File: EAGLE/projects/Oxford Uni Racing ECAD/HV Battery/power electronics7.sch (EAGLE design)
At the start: 49 parts, among them IC1 4043D, IC2 SE555D, IC6 4011D, K1 T9AS1D12-48=T9A, K2 T9AS5D12-12=T9A, K3 T9AS1D12-48=T9A, K4 T9AS1D12-48=T9A, K5 T9AS1D12-48=T9A, Q1 BSS138, Q2 BSS138, Q3 BSS138

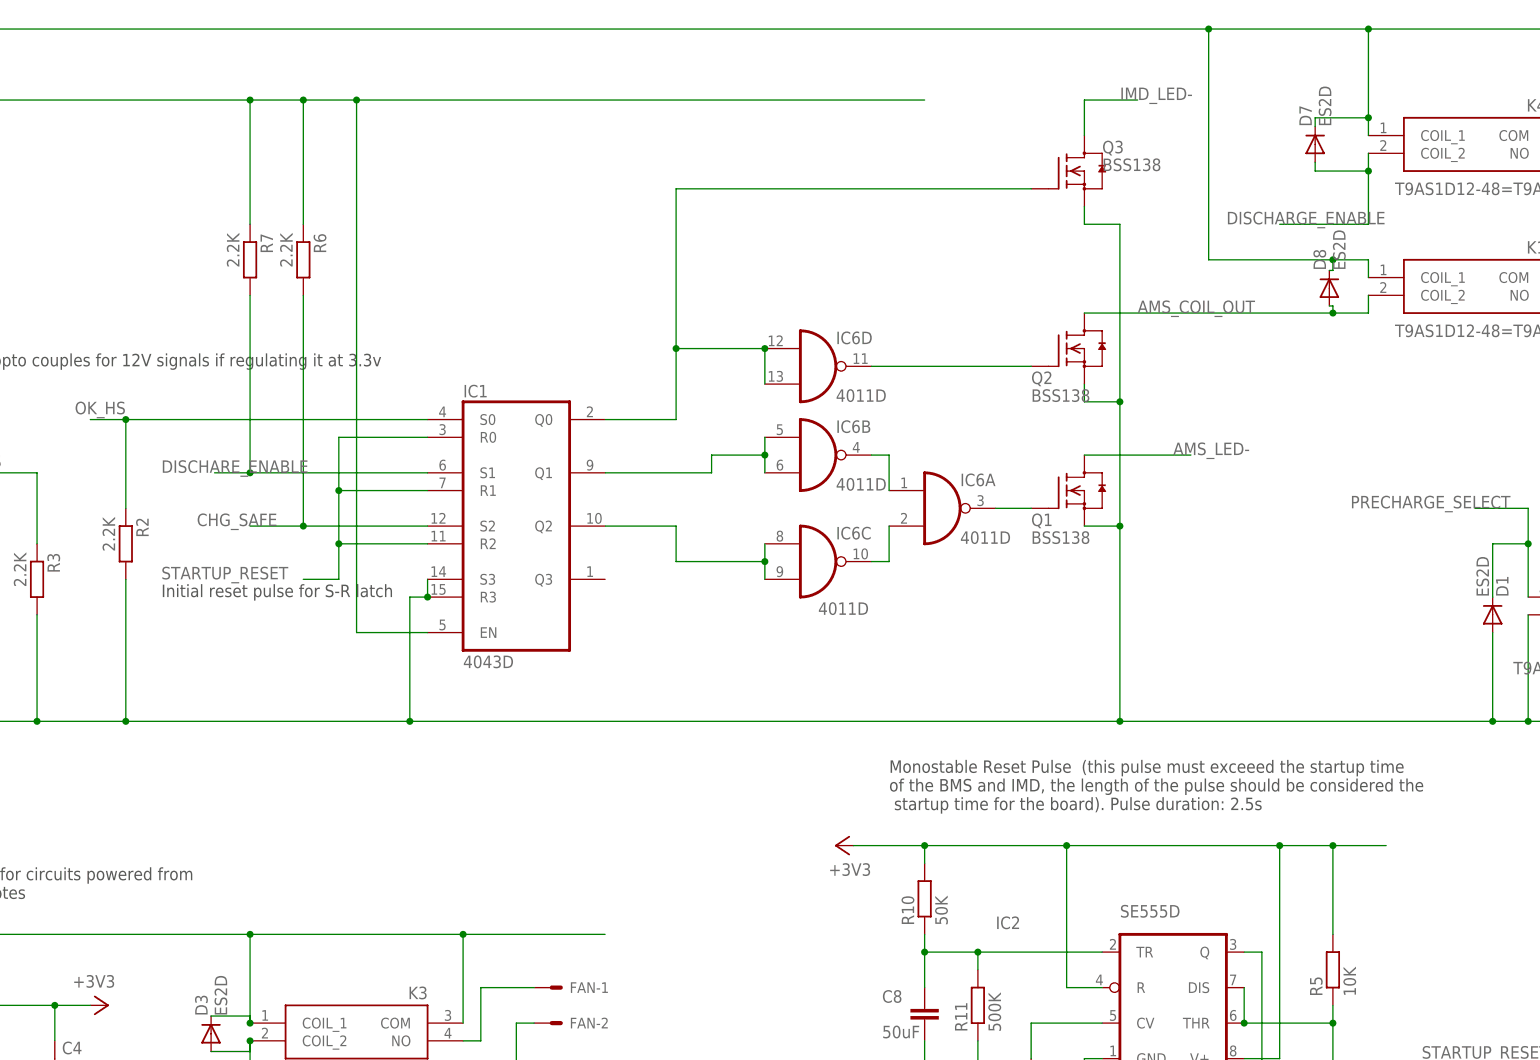
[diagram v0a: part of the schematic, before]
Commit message: added wills suggestions and test pads
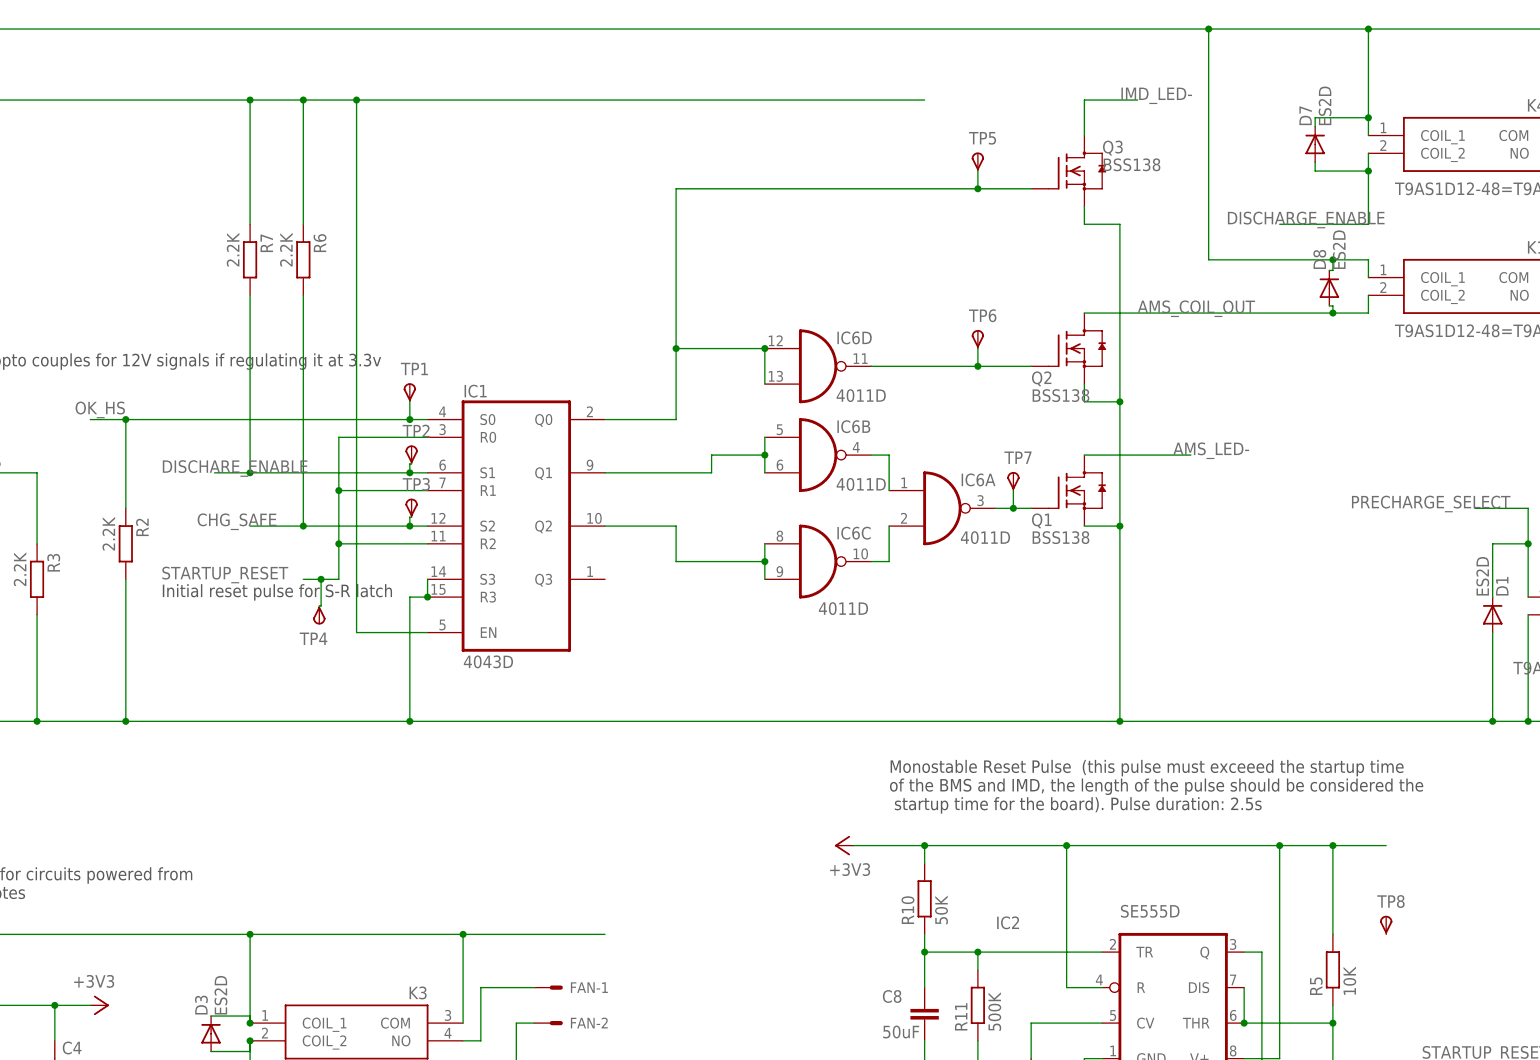
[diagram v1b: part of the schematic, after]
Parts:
- added TP1, TP2, TP3, TP4, TP5, TP6, TP7: TPSTP11R, testpad:TPSTP11R
- added TP8: TPSTP17R, testpad:TPSTP17R
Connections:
- net CHG_SAFE: now also TP3.PP
- net DISCHARE_ENABLE: now also TP2.PP
- net N$21: now also TP7.PP
- net N$37: now also TP6.PP
- net N$8: now also TP5.PP
- net OK_HS: now also TP1.PP
- net STARTUP_RESET: now also TP4.PP
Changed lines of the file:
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@@
 <part name="FAN" library="con-molex" library_urn="urn:adsk.eagle:library:165" deviceset="KK-156-2" device=""/>
 <part name="D3" library="diode" library_urn="urn:adsk.eagle:library:210" deviceset="ES2D" device="" package3d_urn="urn:adsk.eagle:package:43404/2"/>
+<part name="TP1" library="testpad" library_urn="urn:adsk.eagle:library:385" deviceset="TPS" device="TP11R" package3d_urn="urn:adsk.eagle:package:27961/1" value="TPSTP11R"/>
+<part name="TP2" library="testpad" library_urn="urn:adsk.eagle:library:385" deviceset="TPS" device="TP11R" package3d_urn="urn:adsk.eagle:package:27961/1" value="TPSTP11R"/>
+<part name="TP3" library="testpad" library_urn="urn:adsk.eagle:library:385" deviceset="TPS" device="TP11R" package3d_urn="urn:adsk.eagle:package:27961/1" value="TPSTP11R"/>
+<part name="TP5" library="testpad" library_urn="urn:adsk.eagle:library:385" deviceset="TPS" device="TP11R" package3d_urn="urn:adsk.eagle:package:27961/1" value="TPSTP11R"/>
+<part name="TP6" library="testpad" library_urn="urn:adsk.eagle:library:385" deviceset="TPS" device="TP11R" package3d_urn="urn:adsk.eagle:package:27961/1" value="TPSTP11R"/>
+<part name="TP7" library="testpad" library_urn="urn:adsk.eagle:library:385" deviceset="TPS" device="TP11R" package3d_urn="urn:adsk.eagle:package:27961/1" value="TPSTP11R"/>
+<part name="TP8" library="testpad" library_urn="urn:adsk.eagle:library:385" deviceset="TPS" device="TP17R" package3d_urn="urn:adsk.eagle:package:27971/1"/>
+<part name="TP4" library="testpad" library_urn="urn:adsk.eagle:library:385" deviceset="TPS" device="TP11R" package3d_urn="urn:adsk.eagle:package:27961/1" value="TPSTP11R"/>
 </parts>
 <sheets>
@@
 <attribute name="VALUE" x="11.9634" y="-39.624" size="1.778" layer="96" rot="R90"/>
 </instance>
+<instance part="TP1" gate="G$1" x="38.1" y="50.8" smashed="yes">
+<attribute name="NAME" x="36.83" y="52.07" size="1.778" layer="95"/>
+<attribute name="TP_SIGNAL_NAME" x="39.37" y="49.53" size="1.778" layer="97"/>
+</instance>
+<instance part="TP2" gate="G$1" x="38.354" y="41.91" smashed="yes">
+<attribute name="NAME" x="37.084" y="43.18" size="1.778" layer="95"/>
+<attribute name="TP_SIGNAL_NAME" x="39.624" y="40.64" size="1.778" layer="97"/>
+</instance>
+<instance part="TP3" gate="G$1" x="38.354" y="34.29" smashed="yes">
+<attribute name="NAME" x="37.084" y="35.56" size="1.778" layer="95"/>
+<attribute name="TP_SIGNAL_NAME" x="39.624" y="33.02" size="1.778" layer="97"/>
+</instance>
+<instance part="TP5" gate="G$1" x="119.38" y="83.82" smashed="yes">
+<attribute name="NAME" x="118.11" y="85.09" size="1.778" layer="95"/>
+<attribute name="TP_SIGNAL_NAME" x="120.65" y="82.55" size="1.778" layer="97"/>
+</instance>
+<instance part="TP6" gate="G$1" x="119.38" y="58.42" smashed="yes">
+<attribute name="NAME" x="118.11" y="59.69" size="1.778" layer="95"/>
+<attribute name="TP_SIGNAL_NAME" x="120.65" y="57.15" size="1.778" layer="97"/>
+</instance>
+<instance part="TP7" gate="G$1" x="124.46" y="38.1" smashed="yes">
+<attribute name="NAME" x="123.19" y="39.37" size="1.778" layer="95"/>
+<attribute name="TP_SIGNAL_NAME" x="125.73" y="36.83" size="1.778" layer="97"/>
+</instance>
+<instance part="TP8" gate="G$1" x="177.8" y="-25.4" smashed="yes">
+<attribute name="NAME" x="176.53" y="-24.13" size="1.778" layer="95"/>
+<attribute name="TP_SIGNAL_NAME" x="179.07" y="-26.67" size="1.778" layer="97"/>
+</instance>
+<instance part="TP4" gate="G$1" x="25.146" y="16.51" smashed="yes" rot="R180">
+<attribute name="NAME" x="26.416" y="15.24" size="1.778" layer="95" rot="R180"/>
+<attribute name="TP_SIGNAL_NAME" x="23.876" y="17.78" size="1.778" layer="97" rot="R180"/>
+</instance>
 </instances>
 <busses>
@@
 <segment>
 <pinref part="IC1" gate="A" pin="S2"/>
-<wire x1="40.64" y1="30.48" x2="22.86" y2="30.48" width="0.1524" layer="91"/>
+<wire x1="40.64" y1="30.48" x2="38.1" y2="30.48" width="0.1524" layer="91"/>
 <label x="7.62" y="30.48" size="1.778" layer="95"/>
 <pinref part="R6" gate="G$1" pin="2"/>
+<wire x1="38.1" y1="30.48" x2="22.86" y2="30.48" width="0.1524" layer="91"/>
 <wire x1="22.86" y1="30.48" x2="15.24" y2="30.48" width="0.1524" layer="91"/>
 <wire x1="22.86" y1="63.5" x2="22.86" y2="30.48" width="0.1524" layer="91"/>
 <junction x="22.86" y="30.48"/>
+<pinref part="TP3" gate="G$1" pin="PP"/>
+<wire x1="38.354" y1="31.75" x2="38.1" y2="31.75" width="0.1524" layer="91"/>
+<wire x1="38.1" y1="31.75" x2="38.1" y2="30.48" width="0.1524" layer="91"/>
+<junction x="38.1" y="30.48"/>
 </segment>
 </net>
@@
 <segment>
 <pinref part="IC1" gate="A" pin="S0"/>
-<wire x1="40.64" y1="45.72" x2="-2.54" y2="45.72" width="0.1524" layer="91"/>
+<wire x1="40.64" y1="45.72" x2="38.1" y2="45.72" width="0.1524" layer="91"/>
 <pinref part="R2" gate="G$1" pin="1"/>
+<wire x1="38.1" y1="45.72" x2="-2.54" y2="45.72" width="0.1524" layer="91"/>
 <wire x1="-2.54" y1="33.02" x2="-2.54" y2="45.72" width="0.1524" layer="91"/>
 <wire x1="-2.54" y1="45.72" x2="-7.62" y2="45.72" width="0.1524" layer="91"/>
 <label x="-2.54" y="48.26" size="1.778" layer="95" rot="R180"/>
 <junction x="-2.54" y="45.72"/>
+<pinref part="TP1" gate="G$1" pin="PP"/>
+<wire x1="38.1" y1="48.26" x2="38.1" y2="45.72" width="0.1524" layer="91"/>
+<junction x="38.1" y="45.72"/>
 </segment>
 <segment>
@@
 <segment>
 <pinref part="IC6" gate="D" pin="O"/>
-<wire x1="104.14" y1="53.34" x2="127" y2="53.34" width="0.1524" layer="91"/>
+<wire x1="104.14" y1="53.34" x2="119.38" y2="53.34" width="0.1524" layer="91"/>
 <pinref part="Q2" gate="G$1" pin="G"/>
+<pinref part="TP6" gate="G$1" pin="PP"/>
+<wire x1="119.38" y1="53.34" x2="127" y2="53.34" width="0.1524" layer="91"/>
+<wire x1="119.38" y1="55.88" x2="119.38" y2="53.34" width="0.1524" layer="91"/>
+<junction x="119.38" y="53.34"/>
 </segment>
 </net>
@@
 <wire x1="27.94" y1="27.94" x2="27.94" y2="22.86" width="0.1524" layer="91"/>
 <label x="2.54" y="22.86" size="1.778" layer="95"/>
-<wire x1="27.94" y1="22.86" x2="22.86" y2="22.86" width="0.1524" layer="91"/>
+<wire x1="27.94" y1="22.86" x2="25.4" y2="22.86" width="0.1524" layer="91"/>
+<pinref part="TP4" gate="G$1" pin="PP"/>
+<wire x1="25.4" y1="22.86" x2="22.86" y2="22.86" width="0.1524" layer="91"/>
+<wire x1="25.146" y1="19.05" x2="25.4" y2="19.05" width="0.1524" layer="91"/>
+<wire x1="25.4" y1="19.05" x2="25.4" y2="22.86" width="0.1524" layer="91"/>
+<junction x="25.4" y="22.86"/>
 </segment>
 <segment>
@@
 <segment>
 <pinref part="IC6" gate="A" pin="O"/>
-<wire x1="121.92" y1="33.02" x2="127" y2="33.02" width="0.1524" layer="91"/>
+<wire x1="121.92" y1="33.02" x2="124.46" y2="33.02" width="0.1524" layer="91"/>
 <pinref part="Q1" gate="G$1" pin="G"/>
+<pinref part="TP7" gate="G$1" pin="PP"/>
+<wire x1="124.46" y1="33.02" x2="127" y2="33.02" width="0.1524" layer="91"/>
+<wire x1="124.46" y1="35.56" x2="124.46" y2="33.02" width="0.1524" layer="91"/>
+<junction x="124.46" y="33.02"/>
 </segment>
 </net>
@@
 <segment>
 <pinref part="IC1" gate="A" pin="S1"/>
-<wire x1="40.64" y1="38.1" x2="15.24" y2="38.1" width="0.1524" layer="91"/>
+<wire x1="40.64" y1="38.1" x2="38.1" y2="38.1" width="0.1524" layer="91"/>
 <label x="2.54" y="38.1" size="1.778" layer="95"/>
 <pinref part="R7" gate="G$1" pin="2"/>
+<wire x1="38.1" y1="38.1" x2="15.24" y2="38.1" width="0.1524" layer="91"/>
 <wire x1="15.24" y1="63.5" x2="15.24" y2="38.1" width="0.1524" layer="91"/>
 <wire x1="15.24" y1="38.1" x2="10.16" y2="38.1" width="0.1524" layer="91"/>
 <junction x="15.24" y="38.1"/>
+<pinref part="TP2" gate="G$1" pin="PP"/>
+<wire x1="38.354" y1="39.37" x2="38.1" y2="39.37" width="0.1524" layer="91"/>
+<wire x1="38.1" y1="39.37" x2="38.1" y2="38.1" width="0.1524" layer="91"/>
+<junction x="38.1" y="38.1"/>
 </segment>
 </net>
@@
 <pinref part="Q3" gate="G$1" pin="G"/>
 <wire x1="76.2" y1="55.88" x2="76.2" y2="78.74" width="0.1524" layer="91"/>
-<wire x1="127" y1="78.74" x2="76.2" y2="78.74" width="0.1524" layer="91"/>
+<wire x1="127" y1="78.74" x2="119.38" y2="78.74" width="0.1524" layer="91"/>
+<wire x1="119.38" y1="78.74" x2="76.2" y2="78.74" width="0.1524" layer="91"/>
 <wire x1="76.2" y1="45.72" x2="76.2" y2="55.88" width="0.1524" layer="91"/>
 <junction x="76.2" y="55.88"/>
 <pinref part="IC1" gate="A" pin="Q0"/>
 <wire x1="66.04" y1="45.72" x2="76.2" y2="45.72" width="0.1524" layer="91"/>
-</segment>
-</net>
+<pinref part="TP5" gate="G$1" pin="PP"/>
+<wire x1="119.38" y1="81.28" x2="119.38" y2="78.74" width="0.1524" layer="91"/>
+<junction x="119.38" y="78.74"/>
+</segment>
+</net>
